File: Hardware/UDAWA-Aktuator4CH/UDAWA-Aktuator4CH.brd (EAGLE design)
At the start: 160 x 100 mm, 27 parts

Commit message: #3 perbaikan to do list 1sampai5
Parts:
- removed 5V, AC/DC2, AC/DC3, AC/DC4, C3, C4, RC3, RC4: (no value), con-wago-500:W237-102
- moved F4 366.8 mm to (118.1, 66.0)
- moved F2 342.3 mm to (113.0, 81.3)
- moved F3 340.0 mm to (105.4, 44.5)
- moved F1 332.7 mm to (111.8, 92.7)
- moved RC2 257.5 mm to (72.4, 69.8)
- moved RC1 254.3 mm to (74.9, 85.1)
- moved AC/DC1 203.0 mm to (58.4, 91.4)
- moved C2 145.9 mm to (53.3, 50.8)
- moved C1 138.9 mm to (52.1, 62.2)
- moved CH4 104.1 mm to (48.3, 8.89)
- moved GND 94.8 mm to (7.62, 68.6)
- moved NO3 85.2 mm to (69.8, 12.7)
- moved NO1 75.2 mm to (68.6, 24.1)
- moved CH3 72.4 mm to (36.8, 8.89)
- moved CH2 71.1 mm to (25.4, 8.89)
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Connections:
- removed net N$5: F3.2, RC3.2
- removed net N$7: F4.2, RC4.2
- removed net RC1: AC/DC1.2, F1.1
- removed net RC2: AC/DC2.2, F2.1
- removed net RC3: AC/DC3.2, F3.1
- removed net RC4: AC/DC4.2, F4.1
- new net -R1: AC/DC1.1
- new net N$2: F2.2, RC1.1
- new net N$4: F4.2, RC2.1
- new net VCC: GND.2, U$1.3V3
- new net ~R1: AC/DC1.2, F1.1, F2.1, F3.1, F4.1
- net AC/DC1: no longer AC/DC1.1
- net AC/DC2: no longer AC/DC2.1
- net AC/DC3: no longer AC/DC3.1
- net AC/DC4: no longer AC/DC4.1
- net C2: now also C1.2; no longer C2.1
- net C3: now also C2.1; no longer C3.1
- net C4: now also C2.2; no longer C4.1
- net N$3: now also F3.2; no longer F2.2

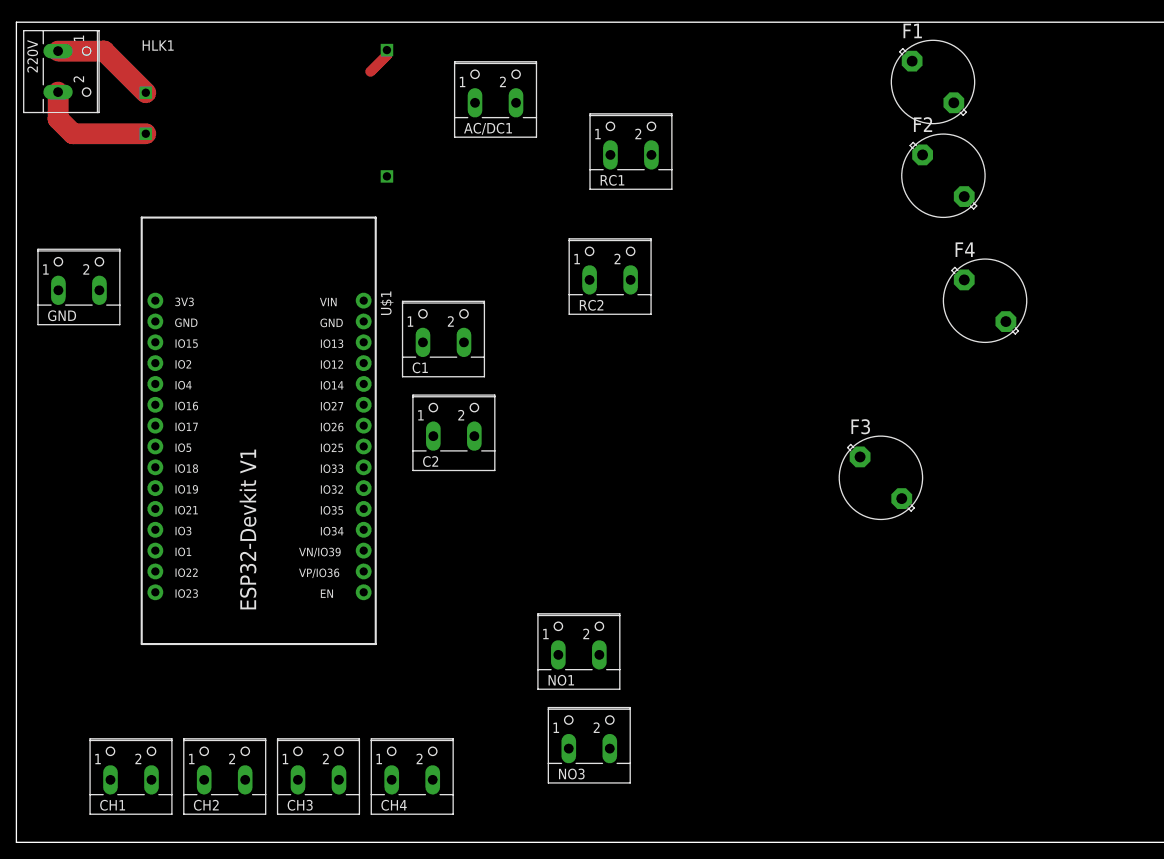
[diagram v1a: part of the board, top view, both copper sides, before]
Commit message: #3 wiring pada mode board dan pastikan penamaan setiap pin dan konektor dibuat dengan jelas dan rapi sesuai diagram.
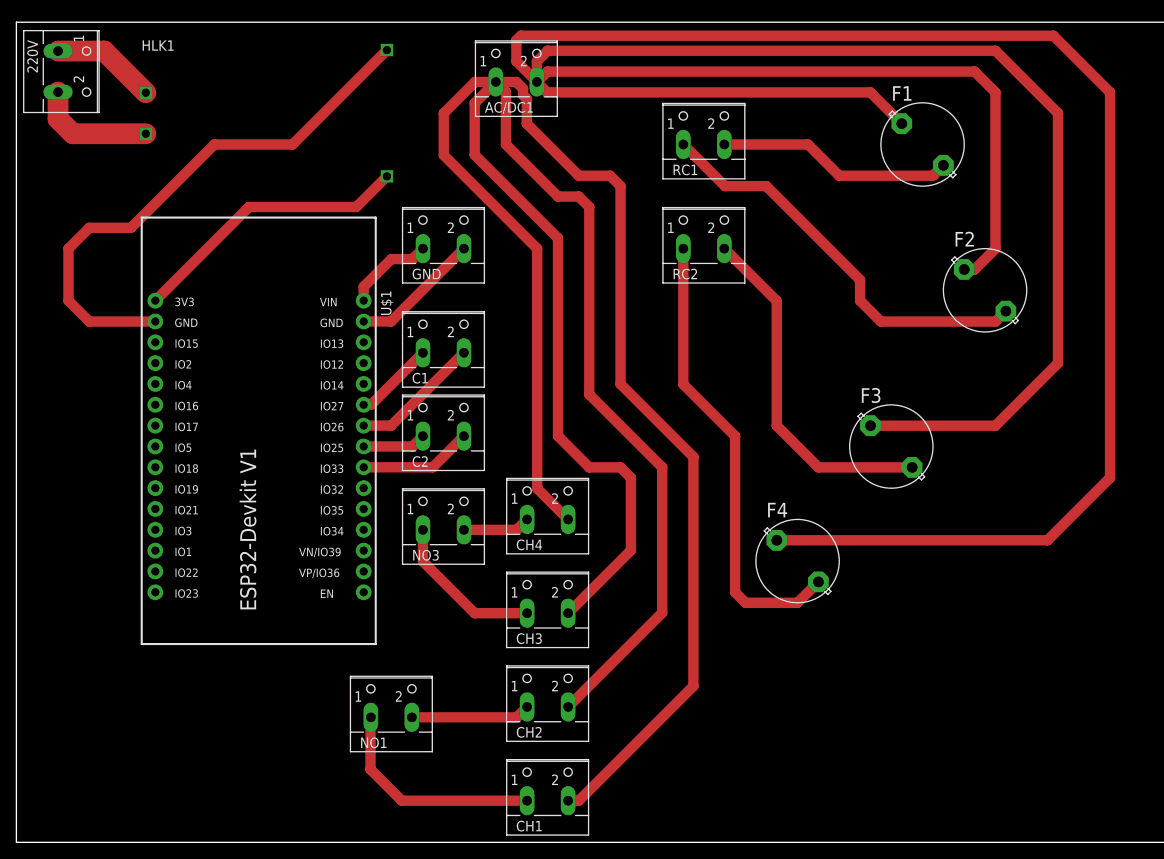
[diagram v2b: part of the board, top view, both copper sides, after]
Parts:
- moved CH1 50.9 mm to (64.8, 6.35)
- moved GND 44.7 mm to (52.1, 73.7)
- moved CH2 40.4 mm to (64.8, 17.8)
- moved F4 39.1 mm to (95.2, 34.3)
- moved CH4 35.8 mm to (64.8, 40.6)
- moved CH3 34.5 mm to (64.8, 29.2)
- moved NO3 32.1 mm to (52.1, 39.4)
- moved NO1 24.1 mm to (45.7, 16.5)
- moved F2 14.9 mm to (118.1, 67.3)
- moved RC2 12.0 mm to (83.8, 73.7)
- moved RC1 8.98 mm to (83.8, 86.4)
- moved F1 7.73 mm to (110.5, 85.1)
- moved F3 4.02 mm to (106.7, 48.3)
- moved AC/DC1 3.59 mm to (61.0, 94.0)
- moved C2 1.27 mm to (52.1, 50.8)
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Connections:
- removed net AC/DC1: CH1.2
- removed net AC/DC2: CH2.2
- removed net AC/DC3: CH3.2
- removed net AC/DC4: CH4.2
- net -R1: now also CH1.2, CH2.2, CH3.2, CH4.2
- net 5V: now also U$1.3V3; no longer U$1.VIN
- net GND: now also U$1.GND@2; no longer U$1.GND@1
- net GND2: now also GND.2, U$1.GND@1; no longer GND.1, U$1.GND@2
- net VCC: now also GND.1, U$1.VIN; no longer GND.2, U$1.3V3
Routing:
- net ~R1: track 0.00 -> 426.6 mm
- net -R1: track 0.00 -> 342.1 mm
- net GND: track 3.45 -> 66.9 mm
- net N$4: track 0.00 -> 56.3 mm
- net N$2: track 0.00 -> 50.3 mm
- net N$3: track 0.00 -> 42.9 mm
- net 5V: track 0.00 -> 34.5 mm
- net N$1: track 0.00 -> 28.8 mm
- net NO1: track 0.00 -> 27.0 mm
- net NO3: track 0.00 -> 19.2 mm
- net GND2: track 0.00 -> 15.9 mm
- net C2: track 0.00 -> 15.9 mm
- net NO2: track 0.00 -> 14.6 mm
- net C4: track 0.00 -> 13.8 mm
- net VCC: track 0.00 -> 10.8 mm
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
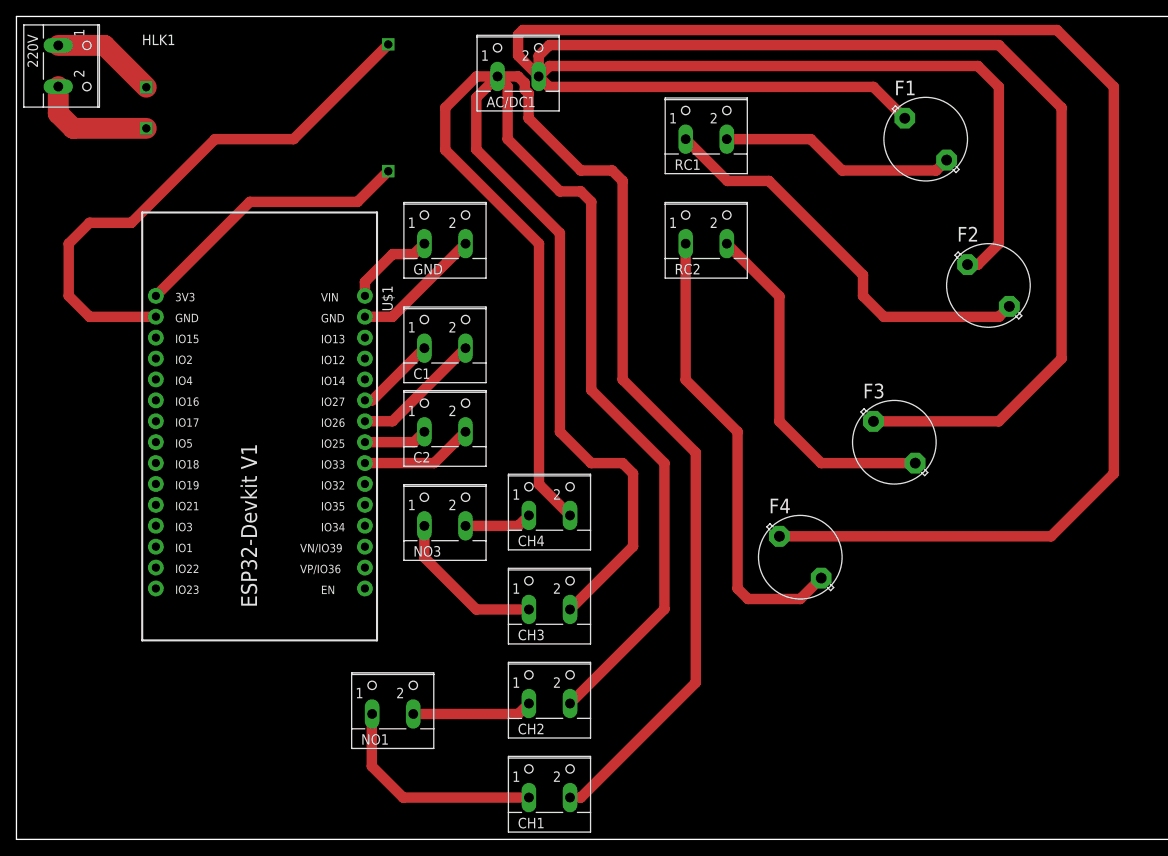
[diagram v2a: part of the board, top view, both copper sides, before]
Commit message: #3 list 8
masih belum lengkap  wiringnya karena kabelnya sudah mentok dan bakalan numpuk kalau dipaksakan
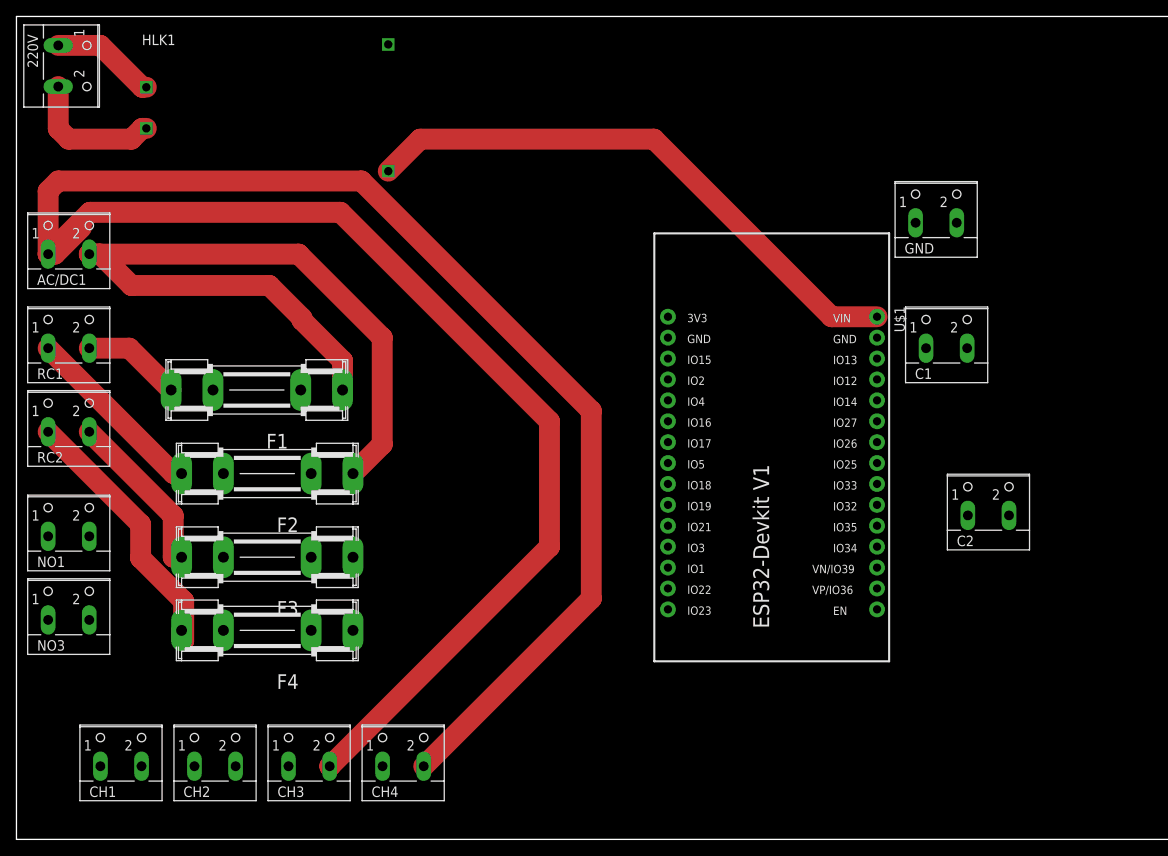
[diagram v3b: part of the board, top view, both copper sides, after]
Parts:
- F1, F2, F3, F4: device fuse:19559 -> fuse:SHK20L
- moved F2 90.6 mm to (30.5, 44.5), turned to 180 degrees
- moved F1 86.8 mm to (29.2, 54.6), turned to 180 degrees
- moved RC1 81.5 mm to (6.35, 61.0)
- moved RC2 80.8 mm to (6.35, 50.8)
- moved F3 77.5 mm to (30.5, 34.3), turned to 180 degrees
- moved C2 66.8 mm to (118.1, 40.6)
- moved F4 65.4 mm to (30.5, 25.4), turned to 180 degrees
- moved U$1 62.3 mm to (91.4, 47.0)
- moved C1 61.0 mm to (113.0, 61.0)
- moved GND 59.7 mm to (111.8, 76.2)
- moved AC/DC1 58.7 mm to (6.35, 72.4)
- moved CH1 52.2 mm to (12.7, 10.2)
- moved NO3 47.1 mm to (6.35, 27.9)
- moved NO1 44.9 mm to (6.35, 38.1)
- moved CH2 41.3 mm to (24.1, 10.2)
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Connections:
- removed net GND2: GND.2, U$1.GND@1
- removed net VCC: GND.1, U$1.VIN
- net 5V: now also GND.1, U$1.VIN; no longer U$1.3V3
- net GND: now also GND.2, U$1.GND@1
- net N$1: now also F1.2A; no longer F1.2
- net N$2: now also F2.2A; no longer F2.2
- net N$3: now also F3.2A; no longer F3.2
- net N$4: now also F4.2A; no longer F4.2
- net ~R1: now also F1.1A, F2.1A, F3.1A, F4.1A; no longer F1.1, F2.1, F3.1, F4.1
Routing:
- net ~R1: track 426.6 -> 97.6 mm
- net -R1: track 342.1 -> 269.3 mm
- net GND: track 66.9 -> 0.00 mm
- net 5V: track 34.5 -> 69.9 mm
- net N$2: track 50.3 -> 22.5 mm
- net NO1: track 27.0 -> 0.00 mm
- net N$4: track 56.3 -> 33.6 mm
- net N$3: track 42.9 -> 20.5 mm
- net NO3: track 19.2 -> 0.00 mm
- net N$1: track 28.8 -> 12.1 mm
- net GND2: track 15.9 -> 0.00 mm
- net C2: track 15.9 -> 0.00 mm
- net NO2: track 14.6 -> 0.00 mm
- net C4: track 13.8 -> 0.00 mm
- net VCC: track 10.8 -> 0.00 mm
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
